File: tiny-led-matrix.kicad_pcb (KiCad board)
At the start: 4 copper layers, 25.5 x 11.2 mm, 110 parts, among them J1 TagConnect_TC2030_SWD, U1 STM32F030F4Px

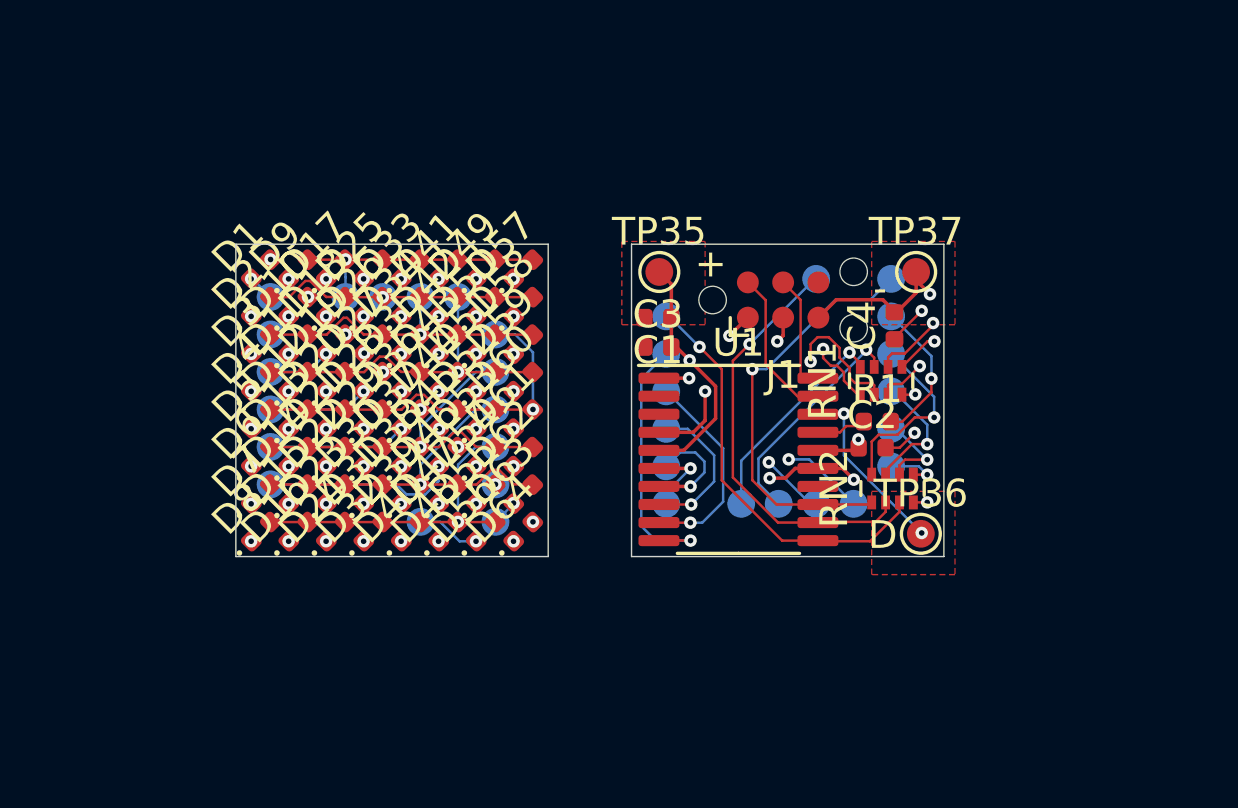
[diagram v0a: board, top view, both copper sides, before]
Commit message: Panelize single unit
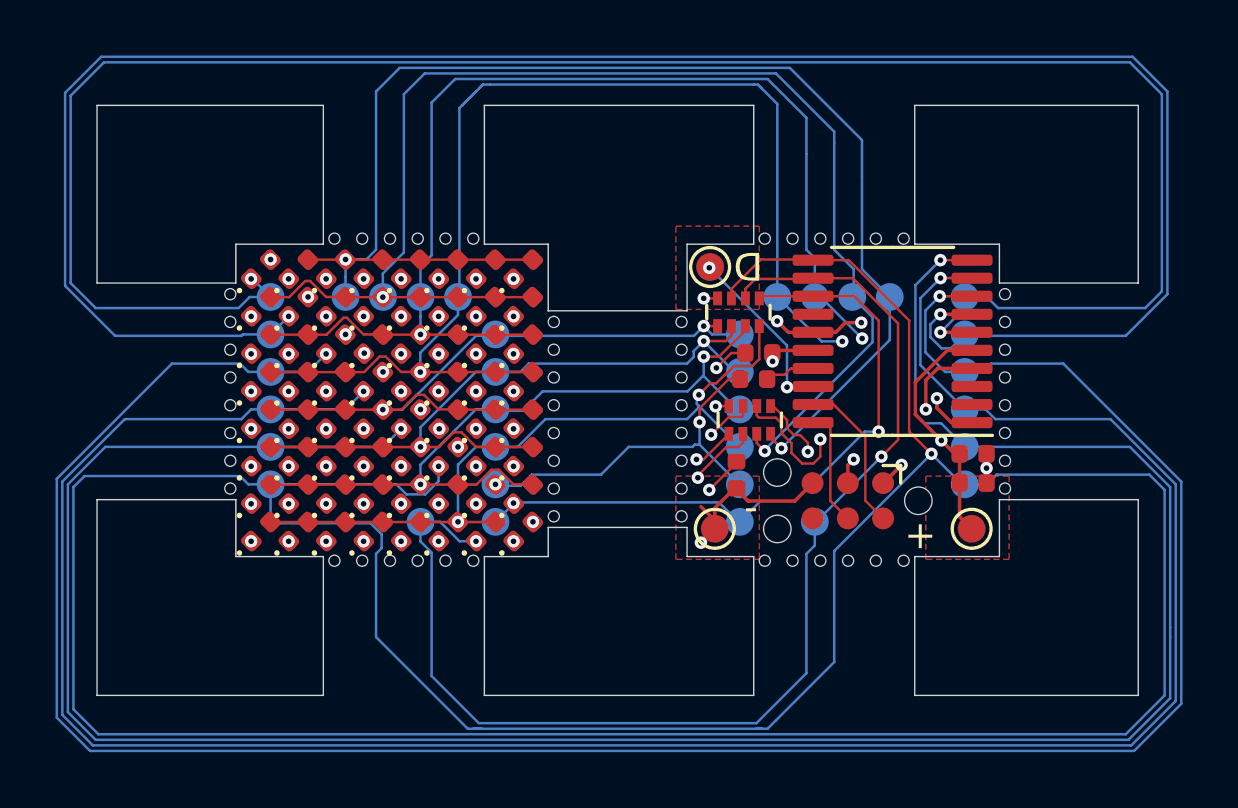
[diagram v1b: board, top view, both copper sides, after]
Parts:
- added REF**: Perforation_0.4mm, Perforation:Perforation_0.4mm, F.Cu at (126.8, 107.9)
- added REF**: Perforation_0.4mm, Perforation:Perforation_0.4mm, F.Cu at (98.9, 103.9)
- added REF**: Perforation_0.4mm, Perforation:Perforation_0.4mm, F.Cu at (98.9, 102.9)
- added REF**: Perforation_0.4mm, Perforation:Perforation_0.4mm, F.Cu at (98.9, 101.9)
- added REF**: Perforation_0.4mm, Perforation:Perforation_0.4mm, F.Cu at (98.9, 107.9)
- added REF**: Perforation_0.4mm, Perforation:Perforation_0.4mm, F.Cu at (98.9, 104.9)
- added REF**: Perforation_0.4mm, Perforation:Perforation_0.4mm, F.Cu at (98.9, 105.9)
- added REF**: Perforation_0.4mm, Perforation:Perforation_0.4mm, F.Cu at (98.9, 106.9)
- added REF**: Perforation_0.4mm, Perforation:Perforation_0.4mm, F.Cu at (102.7, 110.5)
- added REF**: Perforation_0.4mm, Perforation:Perforation_0.4mm, F.Cu at (107.7, 110.5)
- added REF**: Perforation_0.4mm, Perforation:Perforation_0.4mm, F.Cu at (103.7, 110.5)
- added REF**: Perforation_0.4mm, Perforation:Perforation_0.4mm, F.Cu at (126.8, 104.9)
- added REF**: Perforation_0.4mm, Perforation:Perforation_0.4mm, F.Cu at (104.7, 110.5)
- added REF**: Perforation_0.4mm, Perforation:Perforation_0.4mm, F.Cu at (106.7, 110.5)
- added REF**: Perforation_0.4mm, Perforation:Perforation_0.4mm, F.Cu at (105.7, 110.5)
- added REF**: Perforation_0.4mm, Perforation:Perforation_0.4mm, F.Cu at (118.2, 110.5)
- added REF**: Perforation_0.4mm, Perforation:Perforation_0.4mm, F.Cu at (123.2, 110.5)
- added REF**: Perforation_0.4mm, Perforation:Perforation_0.4mm, F.Cu at (119.2, 110.5)
- added REF**: Perforation_0.4mm, Perforation:Perforation_0.4mm, F.Cu at (120.2, 110.5)
- added REF**: Perforation_0.4mm, Perforation:Perforation_0.4mm, F.Cu at (122.2, 110.5)
- added REF**: Perforation_0.4mm, Perforation:Perforation_0.4mm, F.Cu at (121.2, 110.5)
- added REF**: Perforation_0.4mm, Perforation:Perforation_0.4mm, F.Cu at (123.2, 98.9)
- added REF**: Perforation_0.4mm, Perforation:Perforation_0.4mm, F.Cu at (126.8, 105.9)
- added REF**: Perforation_0.4mm, Perforation:Perforation_0.4mm, F.Cu at (122.2, 98.9)
- added REF**: Perforation_0.4mm, Perforation:Perforation_0.4mm, F.Cu at (121.2, 98.9)
- added REF**: Perforation_0.4mm, Perforation:Perforation_0.4mm, F.Cu at (120.2, 98.9)
- added REF**: Perforation_0.4mm, Perforation:Perforation_0.4mm, F.Cu at (119.2, 98.9)
- added REF**: Perforation_0.4mm, Perforation:Perforation_0.4mm, F.Cu at (118.2, 98.9)
- added REF**: Perforation_0.4mm, Perforation:Perforation_0.4mm, F.Cu at (107.7, 98.9)
- added REF**: Perforation_0.4mm, Perforation:Perforation_0.4mm, F.Cu at (106.7, 98.9)
- added REF**: Perforation_0.4mm, Perforation:Perforation_0.4mm, F.Cu at (105.7, 98.9)
- added REF**: Perforation_0.4mm, Perforation:Perforation_0.4mm, F.Cu at (104.7, 98.9)
- added REF**: Perforation_0.4mm, Perforation:Perforation_0.4mm, F.Cu at (103.7, 98.9)
- added REF**: Perforation_0.4mm, Perforation:Perforation_0.4mm, F.Cu at (126.8, 106.9)
- added REF**: Perforation_0.4mm, Perforation:Perforation_0.4mm, F.Cu at (102.7, 98.9)
- added REF**: Perforation_0.4mm, Perforation:Perforation_0.4mm, F.Cu at (110.5, 101.9)
- added REF**: Perforation_0.4mm, Perforation:Perforation_0.4mm, F.Cu at (110.5, 104.9)
- added REF**: Perforation_0.4mm, Perforation:Perforation_0.4mm, F.Cu at (110.5, 103.9)
- added REF**: Perforation_0.4mm, Perforation:Perforation_0.4mm, F.Cu at (110.5, 102.9)
- added REF**: Perforation_0.4mm, Perforation:Perforation_0.4mm, F.Cu at (110.5, 108.9)
- added REF**: Perforation_0.4mm, Perforation:Perforation_0.4mm, F.Cu at (110.5, 105.9)
- added REF**: Perforation_0.4mm, Perforation:Perforation_0.4mm, F.Cu at (110.5, 106.9)
- added REF**: Perforation_0.4mm, Perforation:Perforation_0.4mm, F.Cu at (110.5, 107.9)
- added REF**: Perforation_0.4mm, Perforation:Perforation_0.4mm, F.Cu at (115.2, 108.9)
- added REF**: Perforation_0.4mm, Perforation:Perforation_0.4mm, F.Cu at (126.8, 100.9)
- added REF**: Perforation_0.4mm, Perforation:Perforation_0.4mm, F.Cu at (115.2, 107.9)
- added REF**: Perforation_0.4mm, Perforation:Perforation_0.4mm, F.Cu at (115.2, 106.9)
- added REF**: Perforation_0.4mm, Perforation:Perforation_0.4mm, F.Cu at (115.2, 105.9)
- added REF**: Perforation_0.4mm, Perforation:Perforation_0.4mm, F.Cu at (115.2, 104.9)
- added REF**: Perforation_0.4mm, Perforation:Perforation_0.4mm, F.Cu at (115.2, 103.9)
- added REF**: Perforation_0.4mm, Perforation:Perforation_0.4mm, F.Cu at (115.2, 102.9)
- added REF**: Perforation_0.4mm, Perforation:Perforation_0.4mm, F.Cu at (115.2, 101.9)
- added REF**: Perforation_0.4mm, Perforation:Perforation_0.4mm, F.Cu at (126.8, 103.9)
- added REF**: Perforation_0.4mm, Perforation:Perforation_0.4mm, F.Cu at (126.8, 102.9)
- added REF**: Perforation_0.4mm, Perforation:Perforation_0.4mm, F.Cu at (126.8, 101.9)
- added REF**: Perforation_0.4mm, Perforation:Perforation_0.4mm, F.Cu at (98.9, 100.9)
- moved TP35 14.6 mm to (125.6, 109.3), turned to 180 degrees
- moved TP27 13.1 mm to (125.3, 101.0), turned to 180 degrees
- moved C1 12.8 mm to (125.7, 107.7), turned to 0 degrees
- moved TP32 12.3 mm to (125.3, 107.7), turned to 180 degrees
- moved TP36 12.2 mm to (116.2, 99.9), turned to 180 degrees
- moved C3 12.0 mm to (125.7, 106.7), turned to 180 degrees
- moved TP28 11.8 mm to (125.3, 102.3), turned to 180 degrees
- moved TP37 11.8 mm to (116.3, 109.3), turned to 180 degrees
- moved TP31 11.3 mm to (125.3, 106.4), turned to 180 degrees
- moved TP29 10.9 mm to (125.3, 103.7), turned to 180 degrees
- moved TP30 10.8 mm to (125.3, 105.0), turned to 180 degrees
- moved TP34 10.3 mm to (117.3, 109.1), turned to 180 degrees
- moved TP18 9.17 mm to (122.7, 101.0), turned to 180 degrees
- moved TP33 8.75 mm to (120.0, 109.1), turned to 180 degrees
- moved RN2 8.43 mm to (117.2, 101.5), turned to 270 degrees
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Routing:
- net /K5: track 31.2 -> 139.3 mm
- net /K2: track 29.2 -> 106.4 mm
- net /K3: track 31.2 -> 105.3 mm
- net /K4: track 33.7 -> 105.7 mm
- net /K1: track 25.1 -> 96.0 mm
- net /K0: track 22.3 -> 91.7 mm
- net /A0: track 17.2 -> 49.3 mm
- net /A1: track 18.1 -> 48.7 mm
- net /A2: track 24.6 -> 52.8 mm
- net /A3: track 24.8 -> 52.2 mm
- net /K6: track 26.9 -> 53.1 mm
- net /A4: track 15.5 -> 24.7 mm
- net /K7: track 25.5 -> 33.9 mm
- net /A5: track 17.0 -> 25.2 mm
- net /A6: track 18.8 -> 26.8 mm
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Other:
- board size 25.5 x 11.2 mm -> 37.5 x 21.2 mm

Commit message: Full panel
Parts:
- added C1: 10uF, Capacitor_SMD:C_0402_1005Metric, F.Cu at (167.2, 81.5)
- added C1: 10uF, Capacitor_SMD:C_0402_1005Metric, F.Cu at (167.2, 55.2)
- added C1: 10uF, Capacitor_SMD:C_0402_1005Metric, F.Cu at (167.2, 107.7)
- added C1: 10uF, Capacitor_SMD:C_0402_1005Metric, F.Cu at (125.7, 55.2)
- added C1: 10uF, Capacitor_SMD:C_0402_1005Metric, F.Cu at (125.7, 81.5)
- added C2: 100nF, Capacitor_SMD:C_0402_1005Metric, F.Cu at (159.4, 76.8)
- added C2: 100nF, Capacitor_SMD:C_0402_1005Metric, F.Cu at (159.4, 50.5)
- added C2: 100nF, Capacitor_SMD:C_0402_1005Metric, F.Cu at (159.4, 103.0)
- added C2: 100nF, Capacitor_SMD:C_0402_1005Metric, F.Cu at (117.9, 50.5)
- added C2: 100nF, Capacitor_SMD:C_0402_1005Metric, F.Cu at (117.9, 76.8)
- added C3: 100nF, Capacitor_SMD:C_0402_1005Metric, F.Cu at (167.2, 54.1)
- added C3: 100nF, Capacitor_SMD:C_0402_1005Metric, F.Cu at (167.2, 80.4)
- added C3: 100nF, Capacitor_SMD:C_0402_1005Metric, F.Cu at (167.2, 106.7)
- added C3: 100nF, Capacitor_SMD:C_0402_1005Metric, F.Cu at (125.7, 54.1)
- added C3: 100nF, Capacitor_SMD:C_0402_1005Metric, F.Cu at (125.7, 80.4)
- added C4: 100nF, Capacitor_SMD:C_0402_1005Metric, F.Cu at (158.6, 81.2)
- added C4: 100nF, Capacitor_SMD:C_0402_1005Metric, F.Cu at (158.6, 54.9)
- added C4: 100nF, Capacitor_SMD:C_0402_1005Metric, F.Cu at (158.6, 107.4)
- added C4: 100nF, Capacitor_SMD:C_0402_1005Metric, F.Cu at (117.1, 54.9)
- added C4: 100nF, Capacitor_SMD:C_0402_1005Metric, F.Cu at (117.1, 81.2)
- added D1: LED, LED_SMD:LED_0402_1005Metric, F.Cu at (141.5, 73.8)
- added D1: LED, LED_SMD:LED_0402_1005Metric, F.Cu at (141.5, 47.5)
- added D1: LED, LED_SMD:LED_0402_1005Metric, F.Cu at (141.5, 100.0)
- added D1: LED, LED_SMD:LED_0402_1005Metric, F.Cu at (100.0, 47.5)
- added D1: LED, LED_SMD:LED_0402_1005Metric, F.Cu at (100.0, 73.8)
- added D10: LED, LED_SMD:LED_0402_1005Metric, F.Cu at (142.8, 48.9)
- added D10: LED, LED_SMD:LED_0402_1005Metric, F.Cu at (142.8, 75.1)
- added D10: LED, LED_SMD:LED_0402_1005Metric, F.Cu at (142.8, 101.3)
- added D10: LED, LED_SMD:LED_0402_1005Metric, F.Cu at (101.3, 48.9)
- added D10: LED, LED_SMD:LED_0402_1005Metric, F.Cu at (101.3, 75.1)
- added D11: LED, LED_SMD:LED_0402_1005Metric, F.Cu at (142.8, 50.2)
- added D11: LED, LED_SMD:LED_0402_1005Metric, F.Cu at (142.8, 76.5)
- added D11: LED, LED_SMD:LED_0402_1005Metric, F.Cu at (142.8, 102.7)
- added D11: LED, LED_SMD:LED_0402_1005Metric, F.Cu at (101.3, 50.2)
- added D11: LED, LED_SMD:LED_0402_1005Metric, F.Cu at (101.3, 76.5)
- added D12: LED, LED_SMD:LED_0402_1005Metric, F.Cu at (142.8, 77.8)
- added D12: LED, LED_SMD:LED_0402_1005Metric, F.Cu at (142.8, 51.5)
- added D12: LED, LED_SMD:LED_0402_1005Metric, F.Cu at (142.8, 104.0)
- added D12: LED, LED_SMD:LED_0402_1005Metric, F.Cu at (101.3, 51.5)
- added D12: LED, LED_SMD:LED_0402_1005Metric, F.Cu at (101.3, 77.8)
- added D13: LED, LED_SMD:LED_0402_1005Metric, F.Cu at (142.8, 52.9)
- added D13: LED, LED_SMD:LED_0402_1005Metric, F.Cu at (142.8, 79.2)
- added D13: LED, LED_SMD:LED_0402_1005Metric, F.Cu at (142.8, 105.4)
- added D13: LED, LED_SMD:LED_0402_1005Metric, F.Cu at (101.3, 52.9)
- added D13: LED, LED_SMD:LED_0402_1005Metric, F.Cu at (101.3, 79.2)
- added D14: LED, LED_SMD:LED_0402_1005Metric, F.Cu at (142.8, 54.2)
- added D14: LED, LED_SMD:LED_0402_1005Metric, F.Cu at (142.8, 80.5)
- added D14: LED, LED_SMD:LED_0402_1005Metric, F.Cu at (142.8, 106.8)
- added D14: LED, LED_SMD:LED_0402_1005Metric, F.Cu at (101.3, 54.2)
- added D14: LED, LED_SMD:LED_0402_1005Metric, F.Cu at (101.3, 80.5)
- added D15: LED, LED_SMD:LED_0402_1005Metric, F.Cu at (142.8, 55.6)
- added D15: LED, LED_SMD:LED_0402_1005Metric, F.Cu at (142.8, 81.8)
- added D15: LED, LED_SMD:LED_0402_1005Metric, F.Cu at (142.8, 108.1)
- added D15: LED, LED_SMD:LED_0402_1005Metric, F.Cu at (101.3, 55.6)
- added D15: LED, LED_SMD:LED_0402_1005Metric, F.Cu at (101.3, 81.8)
- added D16: LED, LED_SMD:LED_0402_1005Metric, F.Cu at (142.8, 57.0)
- added D16: LED, LED_SMD:LED_0402_1005Metric, F.Cu at (142.8, 83.2)
- added D16: LED, LED_SMD:LED_0402_1005Metric, F.Cu at (142.8, 109.5)
- added D16: LED, LED_SMD:LED_0402_1005Metric, F.Cu at (101.3, 57.0)
- added D16: LED, LED_SMD:LED_0402_1005Metric, F.Cu at (101.3, 83.2)
- added D17: LED, LED_SMD:LED_0402_1005Metric, F.Cu at (144.2, 47.5)
- added D17: LED, LED_SMD:LED_0402_1005Metric, F.Cu at (144.2, 73.8)
- added D17: LED, LED_SMD:LED_0402_1005Metric, F.Cu at (144.2, 100.0)
- added D17: LED, LED_SMD:LED_0402_1005Metric, F.Cu at (102.7, 47.5)
- added D17: LED, LED_SMD:LED_0402_1005Metric, F.Cu at (102.7, 73.8)
- added D18: LED, LED_SMD:LED_0402_1005Metric, F.Cu at (144.2, 48.9)
- added D18: LED, LED_SMD:LED_0402_1005Metric, F.Cu at (144.2, 75.1)
- added D18: LED, LED_SMD:LED_0402_1005Metric, F.Cu at (144.2, 101.3)
- added D18: LED, LED_SMD:LED_0402_1005Metric, F.Cu at (102.7, 48.9)
- added D18: LED, LED_SMD:LED_0402_1005Metric, F.Cu at (102.7, 75.1)
- added D19: LED, LED_SMD:LED_0402_1005Metric, F.Cu at (144.2, 76.5)
- added D19: LED, LED_SMD:LED_0402_1005Metric, F.Cu at (144.2, 50.2)
- added D19: LED, LED_SMD:LED_0402_1005Metric, F.Cu at (144.2, 102.7)
- added D19: LED, LED_SMD:LED_0402_1005Metric, F.Cu at (102.7, 50.2)
- added D19: LED, LED_SMD:LED_0402_1005Metric, F.Cu at (102.7, 76.5)
- added D2: LED, LED_SMD:LED_0402_1005Metric, F.Cu at (141.5, 75.1)
- added D2: LED, LED_SMD:LED_0402_1005Metric, F.Cu at (141.5, 48.9)
- added D2: LED, LED_SMD:LED_0402_1005Metric, F.Cu at (141.5, 101.3)
- added D2: LED, LED_SMD:LED_0402_1005Metric, F.Cu at (100.0, 48.9)
- added D2: LED, LED_SMD:LED_0402_1005Metric, F.Cu at (100.0, 75.1)
- added D20: LED, LED_SMD:LED_0402_1005Metric, F.Cu at (144.2, 77.8)
- added D20: LED, LED_SMD:LED_0402_1005Metric, F.Cu at (144.2, 51.5)
- added D20: LED, LED_SMD:LED_0402_1005Metric, F.Cu at (144.2, 104.0)
- added D20: LED, LED_SMD:LED_0402_1005Metric, F.Cu at (102.7, 51.5)
- added D20: LED, LED_SMD:LED_0402_1005Metric, F.Cu at (102.7, 77.8)
- added D21: LED, LED_SMD:LED_0402_1005Metric, F.Cu at (144.2, 79.2)
- added D21: LED, LED_SMD:LED_0402_1005Metric, F.Cu at (144.2, 52.9)
- added D21: LED, LED_SMD:LED_0402_1005Metric, F.Cu at (144.2, 105.4)
- added D21: LED, LED_SMD:LED_0402_1005Metric, F.Cu at (102.7, 52.9)
- added D21: LED, LED_SMD:LED_0402_1005Metric, F.Cu at (102.7, 79.2)
- added D22: LED, LED_SMD:LED_0402_1005Metric, F.Cu at (144.2, 54.2)
- added D22: LED, LED_SMD:LED_0402_1005Metric, F.Cu at (144.2, 80.5)
- added D22: LED, LED_SMD:LED_0402_1005Metric, F.Cu at (144.2, 106.8)
- added D22: LED, LED_SMD:LED_0402_1005Metric, F.Cu at (102.7, 54.2)
- added D22: LED, LED_SMD:LED_0402_1005Metric, F.Cu at (102.7, 80.5)
- added D23: LED, LED_SMD:LED_0402_1005Metric, F.Cu at (144.2, 81.8)
- added D23: LED, LED_SMD:LED_0402_1005Metric, F.Cu at (144.2, 55.6)
- added D23: LED, LED_SMD:LED_0402_1005Metric, F.Cu at (144.2, 108.1)
- added D23: LED, LED_SMD:LED_0402_1005Metric, F.Cu at (102.7, 55.6)
- added D23: LED, LED_SMD:LED_0402_1005Metric, F.Cu at (102.7, 81.8)
- added D24: LED, LED_SMD:LED_0402_1005Metric, F.Cu at (144.2, 57.0)
- added D24: LED, LED_SMD:LED_0402_1005Metric, F.Cu at (144.2, 83.2)
- added D24: LED, LED_SMD:LED_0402_1005Metric, F.Cu at (144.2, 109.5)
- added D24: LED, LED_SMD:LED_0402_1005Metric, F.Cu at (102.7, 57.0)
- added D24: LED, LED_SMD:LED_0402_1005Metric, F.Cu at (102.7, 83.2)
- added D25: LED, LED_SMD:LED_0402_1005Metric, F.Cu at (145.6, 73.8)
- added D25: LED, LED_SMD:LED_0402_1005Metric, F.Cu at (145.6, 47.5)
- added D25: LED, LED_SMD:LED_0402_1005Metric, F.Cu at (145.6, 100.0)
- added D25: LED, LED_SMD:LED_0402_1005Metric, F.Cu at (104.0, 47.5)
- added D25: LED, LED_SMD:LED_0402_1005Metric, F.Cu at (104.0, 73.8)
- added D26: LED, LED_SMD:LED_0402_1005Metric, F.Cu at (145.6, 48.9)
- added D26: LED, LED_SMD:LED_0402_1005Metric, F.Cu at (145.6, 75.1)
- added D26: LED, LED_SMD:LED_0402_1005Metric, F.Cu at (145.6, 101.3)
- added D26: LED, LED_SMD:LED_0402_1005Metric, F.Cu at (104.0, 48.9)
- added D26: LED, LED_SMD:LED_0402_1005Metric, F.Cu at (104.0, 75.1)
- added D27: LED, LED_SMD:LED_0402_1005Metric, F.Cu at (145.6, 50.2)
- added D27: LED, LED_SMD:LED_0402_1005Metric, F.Cu at (145.6, 76.5)
- added D27: LED, LED_SMD:LED_0402_1005Metric, F.Cu at (145.6, 102.7)
- added D27: LED, LED_SMD:LED_0402_1005Metric, F.Cu at (104.0, 50.2)
- added D27: LED, LED_SMD:LED_0402_1005Metric, F.Cu at (104.0, 76.5)
- added D28: LED, LED_SMD:LED_0402_1005Metric, F.Cu at (145.6, 77.8)
- added D28: LED, LED_SMD:LED_0402_1005Metric, F.Cu at (145.6, 51.5)
- added D28: LED, LED_SMD:LED_0402_1005Metric, F.Cu at (145.6, 104.0)
- added D28: LED, LED_SMD:LED_0402_1005Metric, F.Cu at (104.0, 51.5)
- added D28: LED, LED_SMD:LED_0402_1005Metric, F.Cu at (104.0, 77.8)
- added D29: LED, LED_SMD:LED_0402_1005Metric, F.Cu at (145.6, 79.2)
- added D29: LED, LED_SMD:LED_0402_1005Metric, F.Cu at (145.6, 52.9)
- added D29: LED, LED_SMD:LED_0402_1005Metric, F.Cu at (145.6, 105.4)
- added D29: LED, LED_SMD:LED_0402_1005Metric, F.Cu at (104.0, 52.9)
- added D29: LED, LED_SMD:LED_0402_1005Metric, F.Cu at (104.0, 79.2)
- added D3: LED, LED_SMD:LED_0402_1005Metric, F.Cu at (141.5, 76.5)
- added D3: LED, LED_SMD:LED_0402_1005Metric, F.Cu at (141.5, 50.2)
- added D3: LED, LED_SMD:LED_0402_1005Metric, F.Cu at (141.5, 102.7)
- added D3: LED, LED_SMD:LED_0402_1005Metric, F.Cu at (100.0, 50.2)
- added D3: LED, LED_SMD:LED_0402_1005Metric, F.Cu at (100.0, 76.5)
- added D30: LED, LED_SMD:LED_0402_1005Metric, F.Cu at (145.6, 80.5)
- added D30: LED, LED_SMD:LED_0402_1005Metric, F.Cu at (145.6, 54.2)
- added D30: LED, LED_SMD:LED_0402_1005Metric, F.Cu at (145.6, 106.8)
- added D30: LED, LED_SMD:LED_0402_1005Metric, F.Cu at (104.0, 54.2)
- added D30: LED, LED_SMD:LED_0402_1005Metric, F.Cu at (104.0, 80.5)
- added D31: LED, LED_SMD:LED_0402_1005Metric, F.Cu at (145.6, 81.8)
- added D31: LED, LED_SMD:LED_0402_1005Metric, F.Cu at (145.6, 55.6)
- added D31: LED, LED_SMD:LED_0402_1005Metric, F.Cu at (145.6, 108.1)
- added D31: LED, LED_SMD:LED_0402_1005Metric, F.Cu at (104.0, 55.6)
- added D31: LED, LED_SMD:LED_0402_1005Metric, F.Cu at (104.0, 81.8)
- added D32: LED, LED_SMD:LED_0402_1005Metric, F.Cu at (145.6, 83.2)
- added D32: LED, LED_SMD:LED_0402_1005Metric, F.Cu at (145.6, 57.0)
- added D32: LED, LED_SMD:LED_0402_1005Metric, F.Cu at (145.6, 109.5)
- added D32: LED, LED_SMD:LED_0402_1005Metric, F.Cu at (104.0, 57.0)
- added D32: LED, LED_SMD:LED_0402_1005Metric, F.Cu at (104.0, 83.2)
- added D33: LED, LED_SMD:LED_0402_1005Metric, F.Cu at (146.9, 73.8)
- added D33: LED, LED_SMD:LED_0402_1005Metric, F.Cu at (146.9, 47.5)
- added D33: LED, LED_SMD:LED_0402_1005Metric, F.Cu at (146.9, 100.0)
- added D33: LED, LED_SMD:LED_0402_1005Metric, F.Cu at (105.4, 47.5)
- added D33: LED, LED_SMD:LED_0402_1005Metric, F.Cu at (105.4, 73.8)
- added D34: LED, LED_SMD:LED_0402_1005Metric, F.Cu at (146.9, 48.9)
- added D34: LED, LED_SMD:LED_0402_1005Metric, F.Cu at (146.9, 75.1)
- added D34: LED, LED_SMD:LED_0402_1005Metric, F.Cu at (146.9, 101.3)
- added D34: LED, LED_SMD:LED_0402_1005Metric, F.Cu at (105.4, 48.9)
- added D34: LED, LED_SMD:LED_0402_1005Metric, F.Cu at (105.4, 75.1)
- added D35: LED, LED_SMD:LED_0402_1005Metric, F.Cu at (146.9, 50.2)
- added D35: LED, LED_SMD:LED_0402_1005Metric, F.Cu at (146.9, 76.5)
- added D35: LED, LED_SMD:LED_0402_1005Metric, F.Cu at (146.9, 102.7)
- added D35: LED, LED_SMD:LED_0402_1005Metric, F.Cu at (105.4, 50.2)
- added D35: LED, LED_SMD:LED_0402_1005Metric, F.Cu at (105.4, 76.5)
- added D36: LED, LED_SMD:LED_0402_1005Metric, F.Cu at (146.9, 77.8)
- added D36: LED, LED_SMD:LED_0402_1005Metric, F.Cu at (146.9, 51.5)
- added D36: LED, LED_SMD:LED_0402_1005Metric, F.Cu at (146.9, 104.0)
- added D36: LED, LED_SMD:LED_0402_1005Metric, F.Cu at (105.4, 51.5)
- added D36: LED, LED_SMD:LED_0402_1005Metric, F.Cu at (105.4, 77.8)
- added D37: LED, LED_SMD:LED_0402_1005Metric, F.Cu at (146.9, 79.2)
- added D37: LED, LED_SMD:LED_0402_1005Metric, F.Cu at (146.9, 52.9)
- added D37: LED, LED_SMD:LED_0402_1005Metric, F.Cu at (146.9, 105.4)
- added D37: LED, LED_SMD:LED_0402_1005Metric, F.Cu at (105.4, 52.9)
- added D37: LED, LED_SMD:LED_0402_1005Metric, F.Cu at (105.4, 79.2)
- added D38: LED, LED_SMD:LED_0402_1005Metric, F.Cu at (146.9, 80.5)
- added D38: LED, LED_SMD:LED_0402_1005Metric, F.Cu at (146.9, 54.2)
- added D38: LED, LED_SMD:LED_0402_1005Metric, F.Cu at (146.9, 106.8)
- added D38: LED, LED_SMD:LED_0402_1005Metric, F.Cu at (105.4, 54.2)
- added D38: LED, LED_SMD:LED_0402_1005Metric, F.Cu at (105.4, 80.5)
- added D39: LED, LED_SMD:LED_0402_1005Metric, F.Cu at (146.9, 81.8)
- added D39: LED, LED_SMD:LED_0402_1005Metric, F.Cu at (146.9, 55.6)
- added D39: LED, LED_SMD:LED_0402_1005Metric, F.Cu at (146.9, 108.1)
- added D39: LED, LED_SMD:LED_0402_1005Metric, F.Cu at (105.4, 55.6)
- added D39: LED, LED_SMD:LED_0402_1005Metric, F.Cu at (105.4, 81.8)
- added D4: LED, LED_SMD:LED_0402_1005Metric, F.Cu at (141.5, 51.5)
- added D4: LED, LED_SMD:LED_0402_1005Metric, F.Cu at (141.5, 77.8)
- added D4: LED, LED_SMD:LED_0402_1005Metric, F.Cu at (141.5, 104.0)
- added D4: LED, LED_SMD:LED_0402_1005Metric, F.Cu at (100.0, 51.5)
- added D4: LED, LED_SMD:LED_0402_1005Metric, F.Cu at (100.0, 77.8)
- added D40: LED, LED_SMD:LED_0402_1005Metric, F.Cu at (146.9, 83.2)
- added D40: LED, LED_SMD:LED_0402_1005Metric, F.Cu at (146.9, 57.0)
- added D40: LED, LED_SMD:LED_0402_1005Metric, F.Cu at (146.9, 109.5)
- added D40: LED, LED_SMD:LED_0402_1005Metric, F.Cu at (105.4, 57.0)
- added D40: LED, LED_SMD:LED_0402_1005Metric, F.Cu at (105.4, 83.2)
- added D41: LED, LED_SMD:LED_0402_1005Metric, F.Cu at (148.2, 47.5)
- added D41: LED, LED_SMD:LED_0402_1005Metric, F.Cu at (148.2, 73.8)
- added D41: LED, LED_SMD:LED_0402_1005Metric, F.Cu at (148.2, 100.0)
- added D41: LED, LED_SMD:LED_0402_1005Metric, F.Cu at (106.8, 47.5)
- added D41: LED, LED_SMD:LED_0402_1005Metric, F.Cu at (106.8, 73.8)
- added D42: LED, LED_SMD:LED_0402_1005Metric, F.Cu at (148.2, 48.9)
- added D42: LED, LED_SMD:LED_0402_1005Metric, F.Cu at (148.2, 75.1)
- added D42: LED, LED_SMD:LED_0402_1005Metric, F.Cu at (148.2, 101.3)
- added D42: LED, LED_SMD:LED_0402_1005Metric, F.Cu at (106.8, 48.9)
- added D42: LED, LED_SMD:LED_0402_1005Metric, F.Cu at (106.8, 75.1)
- added D43: LED, LED_SMD:LED_0402_1005Metric, F.Cu at (148.2, 50.2)
- added D43: LED, LED_SMD:LED_0402_1005Metric, F.Cu at (148.2, 76.5)
- added D43: LED, LED_SMD:LED_0402_1005Metric, F.Cu at (148.2, 102.7)
- added D43: LED, LED_SMD:LED_0402_1005Metric, F.Cu at (106.8, 50.2)
- added D43: LED, LED_SMD:LED_0402_1005Metric, F.Cu at (106.8, 76.5)
- added D44: LED, LED_SMD:LED_0402_1005Metric, F.Cu at (148.2, 77.8)
- added D44: LED, LED_SMD:LED_0402_1005Metric, F.Cu at (148.2, 51.5)
- added D44: LED, LED_SMD:LED_0402_1005Metric, F.Cu at (148.2, 104.0)
- added D44: LED, LED_SMD:LED_0402_1005Metric, F.Cu at (106.8, 51.5)
- added D44: LED, LED_SMD:LED_0402_1005Metric, F.Cu at (106.8, 77.8)
- added D45: LED, LED_SMD:LED_0402_1005Metric, F.Cu at (148.2, 52.9)
- added D45: LED, LED_SMD:LED_0402_1005Metric, F.Cu at (148.2, 79.2)
- added D45: LED, LED_SMD:LED_0402_1005Metric, F.Cu at (148.2, 105.4)
- added D45: LED, LED_SMD:LED_0402_1005Metric, F.Cu at (106.8, 52.9)
- added D45: LED, LED_SMD:LED_0402_1005Metric, F.Cu at (106.8, 79.2)
- added D46: LED, LED_SMD:LED_0402_1005Metric, F.Cu at (148.2, 80.5)
- added D46: LED, LED_SMD:LED_0402_1005Metric, F.Cu at (148.2, 54.2)
- added D46: LED, LED_SMD:LED_0402_1005Metric, F.Cu at (148.2, 106.8)
- added D46: LED, LED_SMD:LED_0402_1005Metric, F.Cu at (106.8, 54.2)
- added D46: LED, LED_SMD:LED_0402_1005Metric, F.Cu at (106.8, 80.5)
- added D47: LED, LED_SMD:LED_0402_1005Metric, F.Cu at (148.2, 81.8)
- added D47: LED, LED_SMD:LED_0402_1005Metric, F.Cu at (148.2, 55.6)
- added D47: LED, LED_SMD:LED_0402_1005Metric, F.Cu at (148.2, 108.1)
- added D47: LED, LED_SMD:LED_0402_1005Metric, F.Cu at (106.8, 55.6)
- added D47: LED, LED_SMD:LED_0402_1005Metric, F.Cu at (106.8, 81.8)
- added D48: LED, LED_SMD:LED_0402_1005Metric, F.Cu at (148.2, 83.2)
- added D48: LED, LED_SMD:LED_0402_1005Metric, F.Cu at (148.2, 57.0)
- added D48: LED, LED_SMD:LED_0402_1005Metric, F.Cu at (148.2, 109.5)
- added D48: LED, LED_SMD:LED_0402_1005Metric, F.Cu at (106.8, 57.0)
- added D48: LED, LED_SMD:LED_0402_1005Metric, F.Cu at (106.8, 83.2)
- added D49: LED, LED_SMD:LED_0402_1005Metric, F.Cu at (149.6, 47.5)
- added D49: LED, LED_SMD:LED_0402_1005Metric, F.Cu at (149.6, 73.8)
- added D49: LED, LED_SMD:LED_0402_1005Metric, F.Cu at (149.6, 100.0)
- added D49: LED, LED_SMD:LED_0402_1005Metric, F.Cu at (108.1, 47.5)
- added D49: LED, LED_SMD:LED_0402_1005Metric, F.Cu at (108.1, 73.8)
- added D5: LED, LED_SMD:LED_0402_1005Metric, F.Cu at (141.5, 52.9)
- added D5: LED, LED_SMD:LED_0402_1005Metric, F.Cu at (141.5, 79.2)
- added D5: LED, LED_SMD:LED_0402_1005Metric, F.Cu at (141.5, 105.4)
- added D5: LED, LED_SMD:LED_0402_1005Metric, F.Cu at (100.0, 52.9)
- added D5: LED, LED_SMD:LED_0402_1005Metric, F.Cu at (100.0, 79.2)
- added D50: LED, LED_SMD:LED_0402_1005Metric, F.Cu at (149.6, 48.9)
- added D50: LED, LED_SMD:LED_0402_1005Metric, F.Cu at (149.6, 75.1)
- added D50: LED, LED_SMD:LED_0402_1005Metric, F.Cu at (149.6, 101.3)
- added D50: LED, LED_SMD:LED_0402_1005Metric, F.Cu at (108.1, 48.9)
- added D50: LED, LED_SMD:LED_0402_1005Metric, F.Cu at (108.1, 75.1)
- added D51: LED, LED_SMD:LED_0402_1005Metric, F.Cu at (149.6, 50.2)
- added D51: LED, LED_SMD:LED_0402_1005Metric, F.Cu at (149.6, 76.5)
- added D51: LED, LED_SMD:LED_0402_1005Metric, F.Cu at (149.6, 102.7)
- added D51: LED, LED_SMD:LED_0402_1005Metric, F.Cu at (108.1, 50.2)
- added D51: LED, LED_SMD:LED_0402_1005Metric, F.Cu at (108.1, 76.5)
- added D52: LED, LED_SMD:LED_0402_1005Metric, F.Cu at (149.6, 51.5)
- added D52: LED, LED_SMD:LED_0402_1005Metric, F.Cu at (149.6, 77.8)
- added D52: LED, LED_SMD:LED_0402_1005Metric, F.Cu at (149.6, 104.0)
- added D52: LED, LED_SMD:LED_0402_1005Metric, F.Cu at (108.1, 51.5)
- added D52: LED, LED_SMD:LED_0402_1005Metric, F.Cu at (108.1, 77.8)
- added D53: LED, LED_SMD:LED_0402_1005Metric, F.Cu at (149.6, 52.9)
- added D53: LED, LED_SMD:LED_0402_1005Metric, F.Cu at (149.6, 79.2)
- added D53: LED, LED_SMD:LED_0402_1005Metric, F.Cu at (149.6, 105.4)
- added D53: LED, LED_SMD:LED_0402_1005Metric, F.Cu at (108.1, 52.9)
- added D53: LED, LED_SMD:LED_0402_1005Metric, F.Cu at (108.1, 79.2)
- added D54: LED, LED_SMD:LED_0402_1005Metric, F.Cu at (149.6, 80.5)
- added D54: LED, LED_SMD:LED_0402_1005Metric, F.Cu at (149.6, 54.2)
- added D54: LED, LED_SMD:LED_0402_1005Metric, F.Cu at (149.6, 106.8)
- added D54: LED, LED_SMD:LED_0402_1005Metric, F.Cu at (108.1, 54.2)
- added D54: LED, LED_SMD:LED_0402_1005Metric, F.Cu at (108.1, 80.5)
- added D55: LED, LED_SMD:LED_0402_1005Metric, F.Cu at (149.6, 81.8)
- added D55: LED, LED_SMD:LED_0402_1005Metric, F.Cu at (149.6, 55.6)
- added D55: LED, LED_SMD:LED_0402_1005Metric, F.Cu at (149.6, 108.1)
- added D55: LED, LED_SMD:LED_0402_1005Metric, F.Cu at (108.1, 55.6)
- added D55: LED, LED_SMD:LED_0402_1005Metric, F.Cu at (108.1, 81.8)
- added D56: LED, LED_SMD:LED_0402_1005Metric, F.Cu at (149.6, 83.2)
- added D56: LED, LED_SMD:LED_0402_1005Metric, F.Cu at (149.6, 109.5)
- added D56: LED, LED_SMD:LED_0402_1005Metric, F.Cu at (149.6, 57.0)
- added D56: LED, LED_SMD:LED_0402_1005Metric, F.Cu at (108.1, 57.0)
- added D56: LED, LED_SMD:LED_0402_1005Metric, F.Cu at (108.1, 83.2)
- added D57: LED, LED_SMD:LED_0402_1005Metric, F.Cu at (150.9, 47.5)
- added D57: LED, LED_SMD:LED_0402_1005Metric, F.Cu at (150.9, 73.8)
- added D57: LED, LED_SMD:LED_0402_1005Metric, F.Cu at (150.9, 100.0)
- added D57: LED, LED_SMD:LED_0402_1005Metric, F.Cu at (109.5, 47.5)
- added D57: LED, LED_SMD:LED_0402_1005Metric, F.Cu at (109.5, 73.8)
- added D58: LED, LED_SMD:LED_0402_1005Metric, F.Cu at (150.9, 48.9)
- added D58: LED, LED_SMD:LED_0402_1005Metric, F.Cu at (150.9, 75.1)
- added D58: LED, LED_SMD:LED_0402_1005Metric, F.Cu at (150.9, 101.3)
- added D58: LED, LED_SMD:LED_0402_1005Metric, F.Cu at (109.5, 48.9)
- added D58: LED, LED_SMD:LED_0402_1005Metric, F.Cu at (109.5, 75.1)
- added D59: LED, LED_SMD:LED_0402_1005Metric, F.Cu at (150.9, 50.2)
- added D59: LED, LED_SMD:LED_0402_1005Metric, F.Cu at (150.9, 76.5)
- added D59: LED, LED_SMD:LED_0402_1005Metric, F.Cu at (150.9, 102.7)
- added D59: LED, LED_SMD:LED_0402_1005Metric, F.Cu at (109.5, 50.2)
- added D59: LED, LED_SMD:LED_0402_1005Metric, F.Cu at (109.5, 76.5)
- added D6: LED, LED_SMD:LED_0402_1005Metric, F.Cu at (141.5, 54.2)
- added D6: LED, LED_SMD:LED_0402_1005Metric, F.Cu at (141.5, 80.5)
- added D6: LED, LED_SMD:LED_0402_1005Metric, F.Cu at (141.5, 106.8)
- added D6: LED, LED_SMD:LED_0402_1005Metric, F.Cu at (100.0, 54.2)
- added D6: LED, LED_SMD:LED_0402_1005Metric, F.Cu at (100.0, 80.5)
- added D60: LED, LED_SMD:LED_0402_1005Metric, F.Cu at (150.9, 77.8)
- added D60: LED, LED_SMD:LED_0402_1005Metric, F.Cu at (150.9, 51.5)
- added D60: LED, LED_SMD:LED_0402_1005Metric, F.Cu at (150.9, 104.0)
- added D60: LED, LED_SMD:LED_0402_1005Metric, F.Cu at (109.5, 51.5)
- added D60: LED, LED_SMD:LED_0402_1005Metric, F.Cu at (109.5, 77.8)
- added D61: LED, LED_SMD:LED_0402_1005Metric, F.Cu at (150.9, 52.9)
- added D61: LED, LED_SMD:LED_0402_1005Metric, F.Cu at (150.9, 79.2)
- added D61: LED, LED_SMD:LED_0402_1005Metric, F.Cu at (150.9, 105.4)
- added D61: LED, LED_SMD:LED_0402_1005Metric, F.Cu at (109.5, 52.9)
- added D61: LED, LED_SMD:LED_0402_1005Metric, F.Cu at (109.5, 79.2)
- added D62: LED, LED_SMD:LED_0402_1005Metric, F.Cu at (150.9, 80.5)
- added D62: LED, LED_SMD:LED_0402_1005Metric, F.Cu at (150.9, 54.2)
- added D62: LED, LED_SMD:LED_0402_1005Metric, F.Cu at (150.9, 106.8)
- added D62: LED, LED_SMD:LED_0402_1005Metric, F.Cu at (109.5, 54.2)
- added D62: LED, LED_SMD:LED_0402_1005Metric, F.Cu at (109.5, 80.5)
- added D63: LED, LED_SMD:LED_0402_1005Metric, F.Cu at (150.9, 81.8)
- added D63: LED, LED_SMD:LED_0402_1005Metric, F.Cu at (150.9, 55.6)
- added D63: LED, LED_SMD:LED_0402_1005Metric, F.Cu at (150.9, 108.1)
- added D63: LED, LED_SMD:LED_0402_1005Metric, F.Cu at (109.5, 55.6)
- added D63: LED, LED_SMD:LED_0402_1005Metric, F.Cu at (109.5, 81.8)
- added D64: LED, LED_SMD:LED_0402_1005Metric, F.Cu at (150.9, 83.2)
- added D64: LED, LED_SMD:LED_0402_1005Metric, F.Cu at (150.9, 57.0)
- added D64: LED, LED_SMD:LED_0402_1005Metric, F.Cu at (150.9, 109.5)
- added D64: LED, LED_SMD:LED_0402_1005Metric, F.Cu at (109.5, 57.0)
- added D64: LED, LED_SMD:LED_0402_1005Metric, F.Cu at (109.5, 83.2)
- added D7: LED, LED_SMD:LED_0402_1005Metric, F.Cu at (141.5, 81.8)
- added D7: LED, LED_SMD:LED_0402_1005Metric, F.Cu at (141.5, 55.6)
- added D7: LED, LED_SMD:LED_0402_1005Metric, F.Cu at (141.5, 108.1)
- added D7: LED, LED_SMD:LED_0402_1005Metric, F.Cu at (100.0, 55.6)
- added D7: LED, LED_SMD:LED_0402_1005Metric, F.Cu at (100.0, 81.8)
- added D8: LED, LED_SMD:LED_0402_1005Metric, F.Cu at (141.5, 57.0)
- added D8: LED, LED_SMD:LED_0402_1005Metric, F.Cu at (141.5, 83.2)
- added D8: LED, LED_SMD:LED_0402_1005Metric, F.Cu at (141.5, 109.5)
- added D8: LED, LED_SMD:LED_0402_1005Metric, F.Cu at (100.0, 57.0)
- added D8: LED, LED_SMD:LED_0402_1005Metric, F.Cu at (100.0, 83.2)
- added D9: LED, LED_SMD:LED_0402_1005Metric, F.Cu at (142.8, 73.8)
- added D9: LED, LED_SMD:LED_0402_1005Metric, F.Cu at (142.8, 47.5)
- added D9: LED, LED_SMD:LED_0402_1005Metric, F.Cu at (142.8, 100.0)
- added D9: LED, LED_SMD:LED_0402_1005Metric, F.Cu at (101.3, 47.5)
- added D9: LED, LED_SMD:LED_0402_1005Metric, F.Cu at (101.3, 73.8)
- added J1: TagConnect_TC2030_SWD, Connector:Tag-Connect_TC2030-IDC-NL_2x03_P1.27mm_Vertical, F.Cu at (162.6, 55.8)
- added J1: TagConnect_TC2030_SWD, Connector:Tag-Connect_TC2030-IDC-NL_2x03_P1.27mm_Vertical, F.Cu at (162.6, 82.1)
- added J1: TagConnect_TC2030_SWD, Connector:Tag-Connect_TC2030-IDC-NL_2x03_P1.27mm_Vertical, F.Cu at (162.6, 108.3)
- added J1: TagConnect_TC2030_SWD, Connector:Tag-Connect_TC2030-IDC-NL_2x03_P1.27mm_Vertical, F.Cu at (121.1, 55.8)
- added J1: TagConnect_TC2030_SWD, Connector:Tag-Connect_TC2030-IDC-NL_2x03_P1.27mm_Vertical, F.Cu at (121.1, 82.1)
- added R1: 1kR, Resistor_SMD:R_0402_1005Metric, F.Cu at (159.2, 77.7)
- added R1: 1kR, Resistor_SMD:R_0402_1005Metric, F.Cu at (159.2, 51.5)
- added R1: 1kR, Resistor_SMD:R_0402_1005Metric, F.Cu at (159.2, 104.0)
- added R1: 1kR, Resistor_SMD:R_0402_1005Metric, F.Cu at (117.8, 51.5)
- added R1: 1kR, Resistor_SMD:R_0402_1005Metric, F.Cu at (117.8, 77.7)
- added REF**: ToolingHole_JLCSMT, ToolingHole:ToolingHole_JLCSMT, F.Cu at (174.6, 118.3)
- added REF**: Perforation_0.4mm, Perforation:Perforation_0.4mm, F.Cu at (168.3, 106.9)
- added REF**: Perforation_0.4mm, Perforation:Perforation_0.4mm, F.Cu at (147.2, 98.9)
- added REF**: Perforation_0.4mm, Perforation:Perforation_0.4mm, F.Cu at (144.2, 98.9)
- added REF**: Perforation_0.4mm, Perforation:Perforation_0.4mm, F.Cu at (160.7, 98.9)
- added REF**: Perforation_0.4mm, Perforation:Perforation_0.4mm, F.Cu at (148.2, 110.5)
- added REF**: Perforation_0.4mm, Perforation:Perforation_0.4mm, F.Cu at (161.7, 98.9)
- added REF**: Perforation_0.4mm, Perforation:Perforation_0.4mm, F.Cu at (163.7, 98.9)
- added REF**: Perforation_0.4mm, Perforation:Perforation_0.4mm, F.Cu at (162.7, 110.5)
- added REF**: Perforation_0.4mm, Perforation:Perforation_0.4mm, F.Cu at (140.4, 105.9)
- added REF**: Perforation_0.4mm, Perforation:Perforation_0.4mm, F.Cu at (144.2, 110.5)
- added REF**: Perforation_0.4mm, Perforation:Perforation_0.4mm, F.Cu at (168.3, 105.9)
- added REF**: Perforation_0.4mm, Perforation:Perforation_0.4mm, F.Cu at (161.7, 72.7)
- added REF**: Perforation_0.4mm, Perforation:Perforation_0.4mm, F.Cu at (162.7, 46.4)
- added REF**: Perforation_0.4mm, Perforation:Perforation_0.4mm, F.Cu at (168.3, 52.4)
- added REF**: Perforation_0.4mm, Perforation:Perforation_0.4mm, F.Cu at (147.2, 84.2)
- added REF**: Perforation_0.4mm, Perforation:Perforation_0.4mm, F.Cu at (163.7, 58.0)
- added REF**: Perforation_0.4mm, Perforation:Perforation_0.4mm, F.Cu at (146.2, 46.4)
- added REF**: Perforation_0.4mm, Perforation:Perforation_0.4mm, F.Cu at (162.7, 58.0)
- added REF**: Perforation_0.4mm, Perforation:Perforation_0.4mm, F.Cu at (163.7, 46.4)
- added REF**: Perforation_0.4mm, Perforation:Perforation_0.4mm, F.Cu at (161.7, 46.4)
- added REF**: Perforation_0.4mm, Perforation:Perforation_0.4mm, F.Cu at (148.2, 58.0)
- added REF**: Perforation_0.4mm, Perforation:Perforation_0.4mm, F.Cu at (160.7, 46.4)
- added REF**: Perforation_0.4mm, Perforation:Perforation_0.4mm, F.Cu at (156.7, 103.9)
- added REF**: Perforation_0.4mm, Perforation:Perforation_0.4mm, F.Cu at (144.2, 46.4)
- added REF**: Perforation_0.4mm, Perforation:Perforation_0.4mm, F.Cu at (147.2, 46.4)
- added REF**: Perforation_0.4mm, Perforation:Perforation_0.4mm, F.Cu at (161.7, 58.0)
- added REF**: Perforation_0.4mm, Perforation:Perforation_0.4mm, F.Cu at (160.7, 58.0)
- added REF**: Perforation_0.4mm, Perforation:Perforation_0.4mm, F.Cu at (164.7, 58.0)
- added REF**: Perforation_0.4mm, Perforation:Perforation_0.4mm, F.Cu at (159.7, 58.0)
- added REF**: Perforation_0.4mm, Perforation:Perforation_0.4mm, F.Cu at (156.7, 81.7)
- added REF**: Perforation_0.4mm, Perforation:Perforation_0.4mm, F.Cu at (152.1, 79.7)
- added REF**: Perforation_0.4mm, Perforation:Perforation_0.4mm, F.Cu at (140.4, 51.4)
- added REF**: Perforation_0.4mm, Perforation:Perforation_0.4mm, F.Cu at (146.2, 58.0)
- added REF**: Perforation_0.4mm, Perforation:Perforation_0.4mm, F.Cu at (156.7, 102.9)
- added REF**: Perforation_0.4mm, Perforation:Perforation_0.4mm, F.Cu at (152.1, 49.4)
- added REF**: Perforation_0.4mm, Perforation:Perforation_0.4mm, F.Cu at (152.1, 55.4)
- added REF**: Perforation_0.4mm, Perforation:Perforation_0.4mm, F.Cu at (152.1, 54.4)
- added REF**: Perforation_0.4mm, Perforation:Perforation_0.4mm, F.Cu at (152.1, 53.4)
- added REF**: Perforation_0.4mm, Perforation:Perforation_0.4mm, F.Cu at (152.1, 56.4)
- added REF**: Perforation_0.4mm, Perforation:Perforation_0.4mm, F.Cu at (156.7, 76.7)
- added REF**: Perforation_0.4mm, Perforation:Perforation_0.4mm, F.Cu at (152.1, 50.4)
- added REF**: Perforation_0.4mm, Perforation:Perforation_0.4mm, F.Cu at (152.1, 51.4)
- added REF**: Perforation_0.4mm, Perforation:Perforation_0.4mm, F.Cu at (140.4, 81.7)
- added REF**: Perforation_0.4mm, Perforation:Perforation_0.4mm, F.Cu at (156.7, 78.7)
- added REF**: Perforation_0.4mm, Perforation:Perforation_0.4mm, F.Cu at (156.7, 108.9)
- added REF**: Perforation_0.4mm, Perforation:Perforation_0.4mm, F.Cu at (168.3, 55.4)
- added REF**: Perforation_0.4mm, Perforation:Perforation_0.4mm, F.Cu at (147.2, 58.0)
- added REF**: Perforation_0.4mm, Perforation:Perforation_0.4mm, F.Cu at (152.1, 82.7)
- added REF**: Perforation_0.4mm, Perforation:Perforation_0.4mm, F.Cu at (164.7, 46.4)
- added REF**: Perforation_0.4mm, Perforation:Perforation_0.4mm, F.Cu at (168.3, 50.4)
- added REF**: Perforation_0.4mm, Perforation:Perforation_0.4mm, F.Cu at (168.3, 53.4)
- added REF**: Perforation_0.4mm, Perforation:Perforation_0.4mm, F.Cu at (145.2, 58.0)
- added REF**: Perforation_0.4mm, Perforation:Perforation_0.4mm, F.Cu at (168.3, 48.4)
- added REF**: Perforation_0.4mm, Perforation:Perforation_0.4mm, F.Cu at (168.3, 49.4)
- added REF**: Perforation_0.4mm, Perforation:Perforation_0.4mm, F.Cu at (147.2, 110.5)
- added REF**: Perforation_0.4mm, Perforation:Perforation_0.4mm, F.Cu at (152.1, 77.7)
- added REF**: Perforation_0.4mm, Perforation:Perforation_0.4mm, F.Cu at (159.7, 46.4)
- added REF**: Perforation_0.4mm, Perforation:Perforation_0.4mm, F.Cu at (140.4, 52.4)
- added REF**: Perforation_0.4mm, Perforation:Perforation_0.4mm, F.Cu at (140.4, 49.4)
- added REF**: Perforation_0.4mm, Perforation:Perforation_0.4mm, F.Cu at (140.4, 50.4)
- added REF**: Perforation_0.4mm, Perforation:Perforation_0.4mm, F.Cu at (156.7, 56.4)
- added REF**: Perforation_0.4mm, Perforation:Perforation_0.4mm, F.Cu at (156.7, 50.4)
- added REF**: Perforation_0.4mm, Perforation:Perforation_0.4mm, F.Cu at (156.7, 51.4)
- added REF**: Perforation_0.4mm, Perforation:Perforation_0.4mm, F.Cu at (168.3, 54.4)
- added REF**: Perforation_0.4mm, Perforation:Perforation_0.4mm, F.Cu at (140.4, 54.4)
- added REF**: Perforation_0.4mm, Perforation:Perforation_0.4mm, F.Cu at (140.4, 55.4)
- added REF**: Perforation_0.4mm, Perforation:Perforation_0.4mm, F.Cu at (168.3, 78.7)
- added REF**: Perforation_0.4mm, Perforation:Perforation_0.4mm, F.Cu at (156.7, 52.4)
- added REF**: Perforation_0.4mm, Perforation:Perforation_0.4mm, F.Cu at (168.3, 51.4)
- added REF**: Perforation_0.4mm, Perforation:Perforation_0.4mm, F.Cu at (144.2, 58.0)
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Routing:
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- added copper zone on F.Cu, net (none)
- added copper zone on In1.Cu, net (none)
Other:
- board size 37.5 x 21.2 mm -> 89 x 85 mm
